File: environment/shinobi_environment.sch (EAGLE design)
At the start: 9 parts

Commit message: シルク削除
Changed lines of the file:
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@@
 <?xml version="1.0" encoding="utf-8"?>
 <!DOCTYPE eagle SYSTEM "eagle.dtd">
-<eagle version="8.2.2">
+<eagle version="9.6.0">
 <drawing>
 <settings>
 <setting alwaysvectorfont="no"/>
+<setting keepoldvectorfont="yes"/>
 <setting verticaltext="up"/>
 </settings>
@@
 </plain>
 <instances>
-<instance part="+3V4" gate="G$1" x="63.5" y="73.66"/>
-<instance part="GND10" gate="1" x="48.26" y="45.72"/>
-<instance part="U$1" gate="G$1" x="0" y="0"/>
-<instance part="I2C" gate="G$1" x="30.48" y="63.5"/>
-<instance part="B1" gate="G$1" x="53.34" y="116.84"/>
-<instance part="+3V1" gate="G$1" x="20.32" y="129.54"/>
-<instance part="C1" gate="G$1" x="20.32" y="99.06" rot="R90"/>
-<instance part="GND1" gate="1" x="20.32" y="91.44"/>
-<instance part="GND2" gate="1" x="25.4" y="111.76"/>
-<instance part="+3V2" gate="G$1" x="81.28" y="124.46"/>
-<instance part="GND3" gate="1" x="73.66" y="119.38"/>
-<instance part="GND4" gate="1" x="35.56" y="101.6"/>
-<instance part="IC3" gate="G$1" x="121.92" y="71.12"/>
-<instance part="C3" gate="G$1" x="101.6" y="48.26" rot="R90"/>
-<instance part="R4" gate="G$1" x="147.32" y="83.82" rot="R90"/>
-<instance part="+3V3" gate="G$1" x="101.6" y="96.52"/>
-<instance part="+3V5" gate="G$1" x="147.32" y="96.52"/>
-<instance part="GND5" gate="1" x="101.6" y="38.1"/>
-<instance part="GND6" gate="1" x="142.24" y="38.1"/>
-<instance part="IC1" gate="G$1" x="203.2" y="66.04"/>
-<instance part="R1" gate="G$1" x="175.26" y="81.28" rot="R90"/>
-<instance part="C2" gate="G$1" x="175.26" y="58.42" rot="R90"/>
-<instance part="+3V6" gate="G$1" x="175.26" y="99.06"/>
-<instance part="GND7" gate="1" x="175.26" y="45.72"/>
-<instance part="GND8" gate="1" x="185.42" y="45.72"/>
+<instance part="+3V4" gate="G$1" x="63.5" y="73.66" smashed="yes">
+<attribute name="VALUE" x="60.96" y="68.58" size="1.778" layer="96" rot="R90"/>
+</instance>
+<instance part="GND10" gate="1" x="48.26" y="45.72" smashed="yes">
+<attribute name="VALUE" x="45.72" y="43.18" size="1.778" layer="96"/>
+</instance>
+<instance part="U$1" gate="G$1" x="0" y="0" smashed="yes">
+<attribute name="DRAWING_NAME" x="175.26" y="24.13" size="2.54" layer="94"/>
+<attribute name="LAST_DATE_TIME" x="172.72" y="20.32" size="1.778" layer="94" align="center-left"/>
+<attribute name="SHEET" x="223.52" y="20.32" size="1.778" layer="94" align="center-left"/>
+</instance>
+<instance part="I2C" gate="G$1" x="30.48" y="63.5" smashed="yes">
+<attribute name="NAME" x="22.86" y="74.168" size="1.778" layer="95"/>
+</instance>
+<instance part="B1" gate="G$1" x="53.34" y="116.84" smashed="yes">
+<attribute name="NAME" x="49.53" y="122.428" size="1.27" layer="95"/>
+</instance>
+<instance part="+3V1" gate="G$1" x="20.32" y="129.54" smashed="yes">
+<attribute name="VALUE" x="17.78" y="124.46" size="1.778" layer="96" rot="R90"/>
+</instance>
+<instance part="C1" gate="G$1" x="20.32" y="99.06" smashed="yes" rot="R90">
+<attribute name="NAME" x="18.034" y="96.774" size="1.4224" layer="95" rot="R90"/>
+<attribute name="VALUE" x="22.606" y="96.774" size="1.4224" layer="96" rot="R90" align="top-left"/>
+</instance>
+<instance part="GND1" gate="1" x="20.32" y="91.44" smashed="yes">
+<attribute name="VALUE" x="17.78" y="88.9" size="1.778" layer="96"/>
+</instance>
+<instance part="GND2" gate="1" x="25.4" y="111.76" smashed="yes">
+<attribute name="VALUE" x="22.86" y="109.22" size="1.778" layer="96"/>
+</instance>
+<instance part="+3V2" gate="G$1" x="81.28" y="124.46" smashed="yes">
+<attribute name="VALUE" x="78.74" y="119.38" size="1.778" layer="96" rot="R90"/>
+</instance>
+<instance part="GND3" gate="1" x="73.66" y="119.38" smashed="yes">
+<attribute name="VALUE" x="71.12" y="116.84" size="1.778" layer="96"/>
+</instance>
+<instance part="GND4" gate="1" x="35.56" y="101.6" smashed="yes">
+<attribute name="VALUE" x="33.02" y="99.06" size="1.778" layer="96"/>
+</instance>
+<instance part="IC3" gate="G$1" x="121.92" y="71.12" smashed="yes">
+<attribute name="NAME" x="111.76" y="84.328" size="1.27" layer="95"/>
+</instance>
+<instance part="C3" gate="G$1" x="101.6" y="48.26" smashed="yes" rot="R90">
+<attribute name="NAME" x="99.314" y="45.974" size="1.4224" layer="95" rot="R90"/>
+<attribute name="VALUE" x="103.886" y="45.974" size="1.4224" layer="96" rot="R90" align="top-left"/>
+</instance>
+<instance part="R4" gate="G$1" x="147.32" y="83.82" smashed="yes" rot="R90">
+<attribute name="NAME" x="145.796" y="81.534" size="1.4224" layer="95" rot="R90"/>
+<attribute name="VALUE" x="148.844" y="81.534" size="1.4224" layer="96" rot="R90" align="top-left"/>
+</instance>
+<instance part="+3V3" gate="G$1" x="101.6" y="96.52" smashed="yes">
+<attribute name="VALUE" x="99.06" y="91.44" size="1.778" layer="96" rot="R90"/>
+</instance>
+<instance part="+3V5" gate="G$1" x="147.32" y="96.52" smashed="yes">
+<attribute name="VALUE" x="144.78" y="91.44" size="1.778" layer="96" rot="R90"/>
+</instance>
+<instance part="GND5" gate="1" x="101.6" y="38.1" smashed="yes">
+<attribute name="VALUE" x="99.06" y="35.56" size="1.778" layer="96"/>
+</instance>
+<instance part="GND6" gate="1" x="142.24" y="38.1" smashed="yes">
+<attribute name="VALUE" x="139.7" y="35.56" size="1.778" layer="96"/>
+</instance>
+<instance part="IC1" gate="G$1" x="203.2" y="66.04" smashed="yes">
+<attribute name="NAME" x="195.834" y="74.168" size="1.778" layer="95"/>
+</instance>
+<instance part="R1" gate="G$1" x="175.26" y="81.28" smashed="yes" rot="R90">
+<attribute name="NAME" x="173.736" y="78.994" size="1.4224" layer="95" rot="R90"/>
+<attribute name="VALUE" x="176.784" y="78.994" size="1.4224" layer="96" rot="R90" align="top-left"/>
+</instance>
+<instance part="C2" gate="G$1" x="175.26" y="58.42" smashed="yes" rot="R90">
+<attribute name="NAME" x="172.974" y="56.134" size="1.4224" layer="95" rot="R90"/>
+<attribute name="VALUE" x="177.546" y="56.134" size="1.4224" layer="96" rot="R90" align="top-left"/>
+</instance>
+<instance part="+3V6" gate="G$1" x="175.26" y="99.06" smashed="yes">
+<attribute name="VALUE" x="172.72" y="93.98" size="1.778" layer="96" rot="R90"/>
+</instance>
+<instance part="GND7" gate="1" x="175.26" y="45.72" smashed="yes">
+<attribute name="VALUE" x="172.72" y="43.18" size="1.778" layer="96"/>
+</instance>
+<instance part="GND8" gate="1" x="185.42" y="45.72" smashed="yes">
+<attribute name="VALUE" x="182.88" y="43.18" size="1.778" layer="96"/>
+</instance>
 </instances>
 <busses>
@@
 <compatibility>
 <note version="8.2" severity="warning">
-Since Version 8.2, Eagle supports online libraries. The ids
+Since Version 8.2, EAGLE supports online libraries. The ids
 of those online libraries will not be understood (or retained)
 with this version.

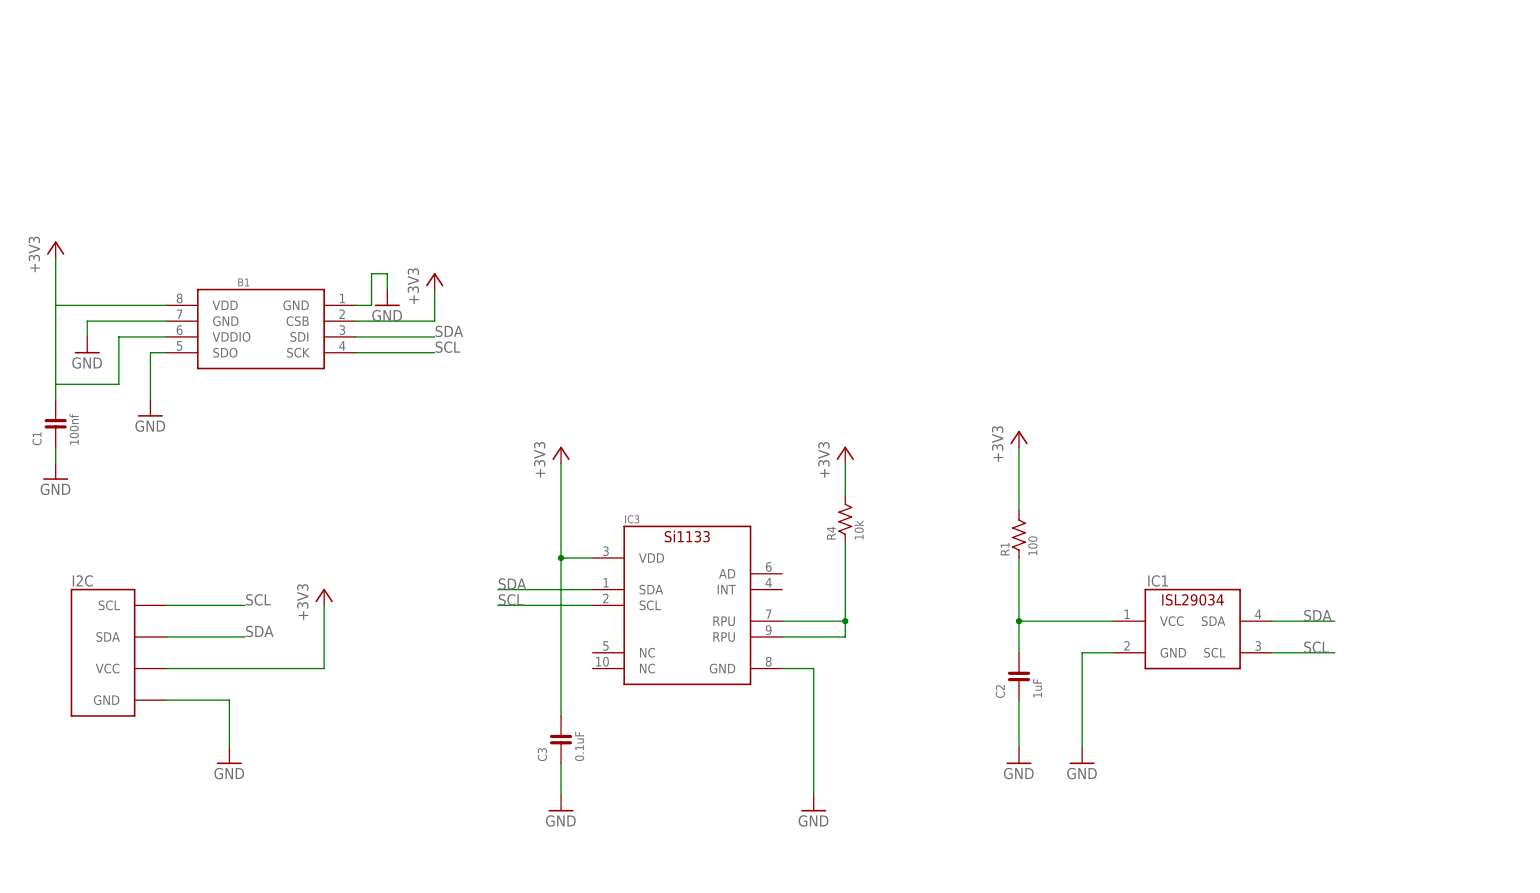
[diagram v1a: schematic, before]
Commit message: #21 Shinobi Enviroment 1.0.1 アップデート　VCC ５V対応　LDO、レベル変換、BME６８０通風口追加、番号の変更　４から２１
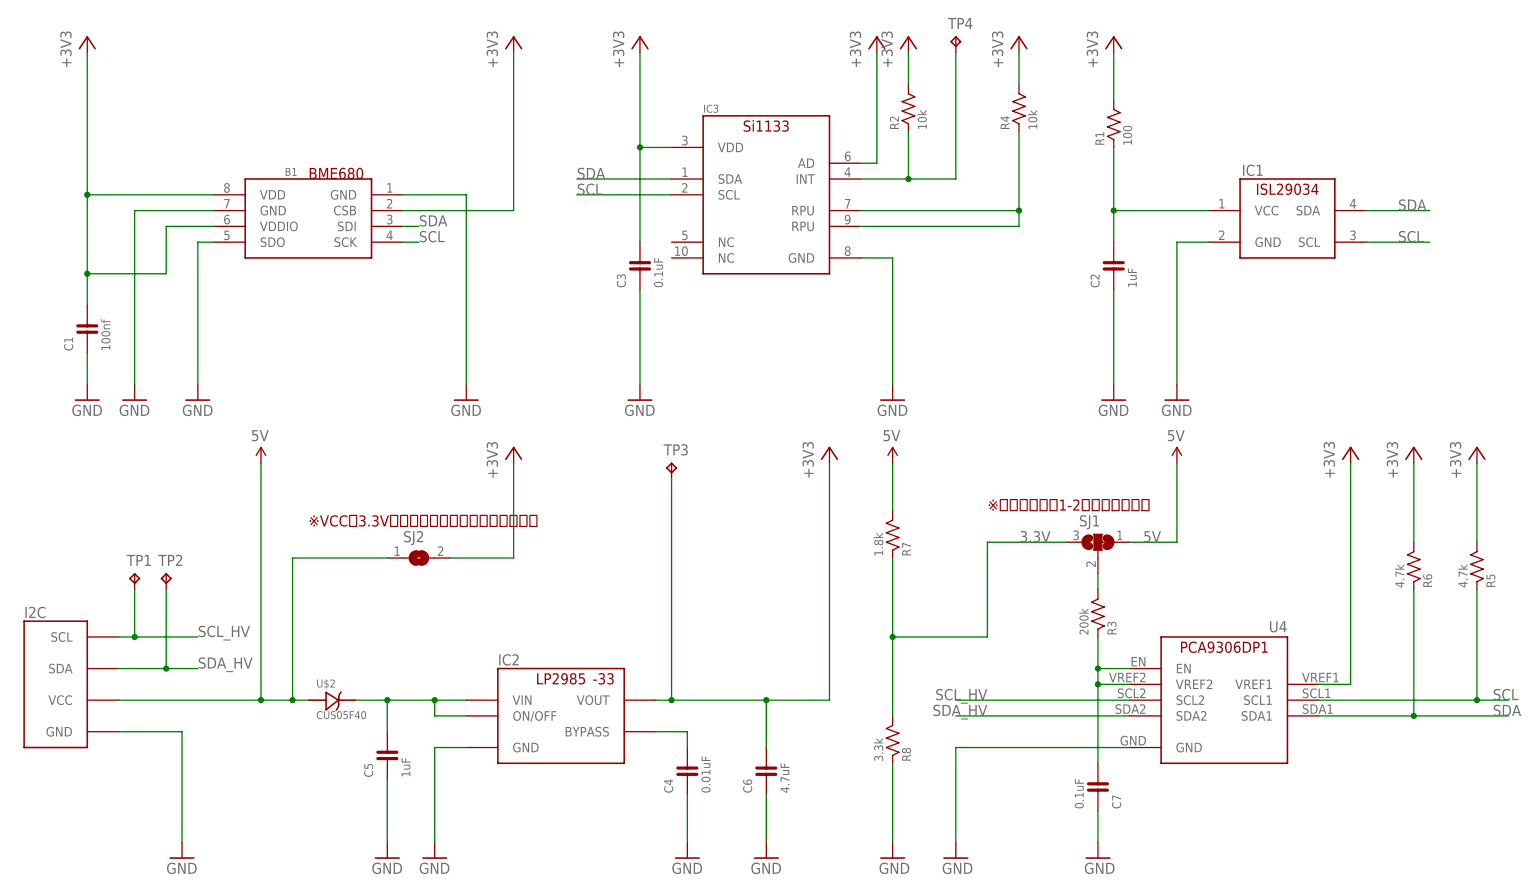
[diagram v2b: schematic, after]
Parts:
- added C4: 0.01uF, FaBo-Capacitor:CAPACITOR-0603
- added C5: 1uF, FaBo-Capacitor:CAPACITOR-0603
- added C6: 4.7uF, FaBo-Capacitor:CAPACITOR-0603
- added C7: 0.1uF, FaBo-Capacitor:CAPACITOR-0603
- added IC2: (no value), FaBo-Supply:LP2985-33DBV
- added R2: 10k, FaBo-Resistors:RESISTOR-0603
- added R3: 200k, FaBo-Resistors:RESISTOR-0603
- added R5, R6: 4.7k, FaBo-Resistors:RESISTOR-0603
- added R7: 1.8k, FaBo-Resistors:RESISTOR-0603
- added R8: 3.3k, FaBo-Resistors:RESISTOR-0603
- added SJ1: (no value), jumper:SJ2W
- added SJ2: (no value), jumper:SJ
- added TP1, TP2, TP3, TP4: TPB1,27, testpad:TPB1,27
- added U$2: CUS05F40, FaBo-Diode:CUS05F40
- added U4: PCA9306DP1, FaBo-LevelTranslator:PCA9306DP1
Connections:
- new net 3.3V: R7.1, R8.2, SJ1.3
- new net 5V: I2C.VCC, R7.2, SJ1.1, SJ2.1, U$2.ANODE
- new net N$2: C4.2, IC2.BYPASS
- new net N$3: C5.2, IC2.ON/OFF, IC2.VIN, U$2.CATHODE
- new net N$5: IC3.INT@4, R2.1, TP4.TP
- new net N$8: C7.2, R3.1, U4.EN, U4.VREF2
- new net N$9: R3.2, SJ1.2
- new net SCL_HV: I2C.SCL, TP1.TP, U4.SCL2
- new net SDA_HV: I2C.SDA, TP2.TP, U4.SDA2
- net +3V3: now also C6.2, IC2.VOUT, IC3.AD@6, R2.2, R5.2, R6.2, SJ2.2, TP3.TP, U4.VREF1; no longer I2C.VCC
- net GND: now also C4.1, C5.1, C6.1, C7.1, IC2.GND, R8.1, U4.GND
- net SCL: now also R5.1, U4.SCL1; no longer I2C.SCL
- net SDA: now also R6.1, U4.SDA1; no longer I2C.SDA
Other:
- note added: "-33"
- note added: "BME680"
- note added: "※VCCが3.3Vの時使用、通常は使用しないこと"
- note added: "※デフォルトで1-2に半田すること"
- moved on the sheet: B1, C1, C2, C3, I2C, IC1, IC3, R1, R4
